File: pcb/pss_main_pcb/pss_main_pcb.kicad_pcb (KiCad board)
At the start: 2 copper layers, 177.8 x 55.9 mm, 96 parts, among them J1 24V DC Input, J2 220V AC Input, J3 Hot Air Gun, J4 Soldering Iron, J5 STM32_Prog, J6 UART_Prog, Q1 BC817, Q2 MMBT2222, Q3 MMBT2907, Q4 IRLML9301T, Q5 IRFZ44S, Q6 BT139B-800, SW1 Hot Air Gun Input, SW2 Soldering Iron Input, SW3 SW_Push, SW4 Main Encoder Input, SW5 EN, SW6 Boot, U1 LM2596S-5, U2 LM2596S-3.3, U3 MOC3023S, U4 LM358, U5 STM32F030K6Tx, U6 ESP32-WROOM-32U, U7 2.8inch_SPI_Module_ILI9341_SK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

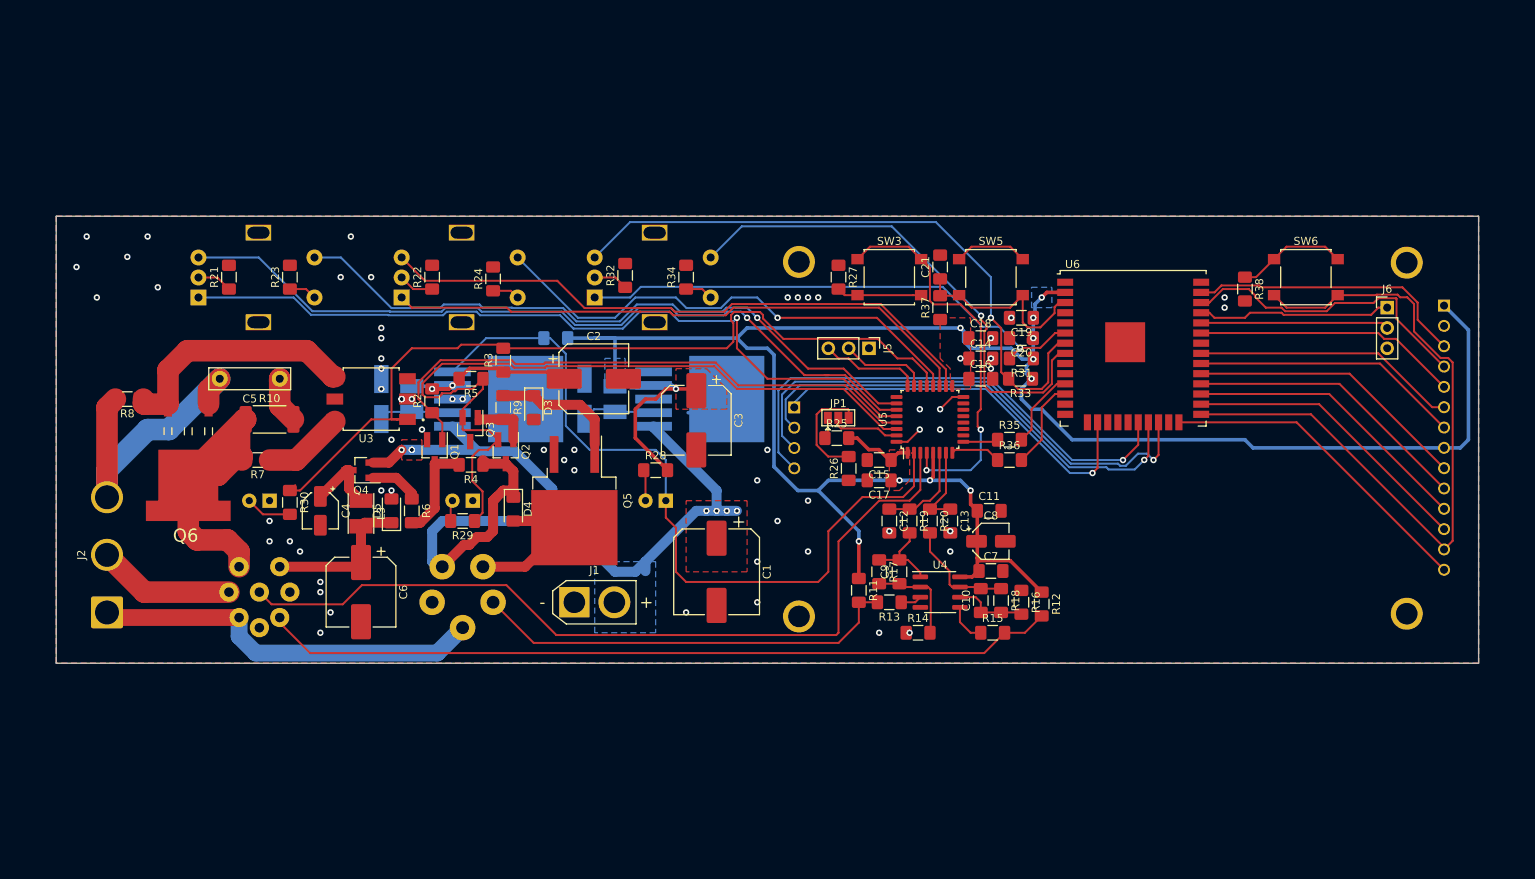
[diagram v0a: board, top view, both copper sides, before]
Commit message: Add 3D models and totaly redesign PCB
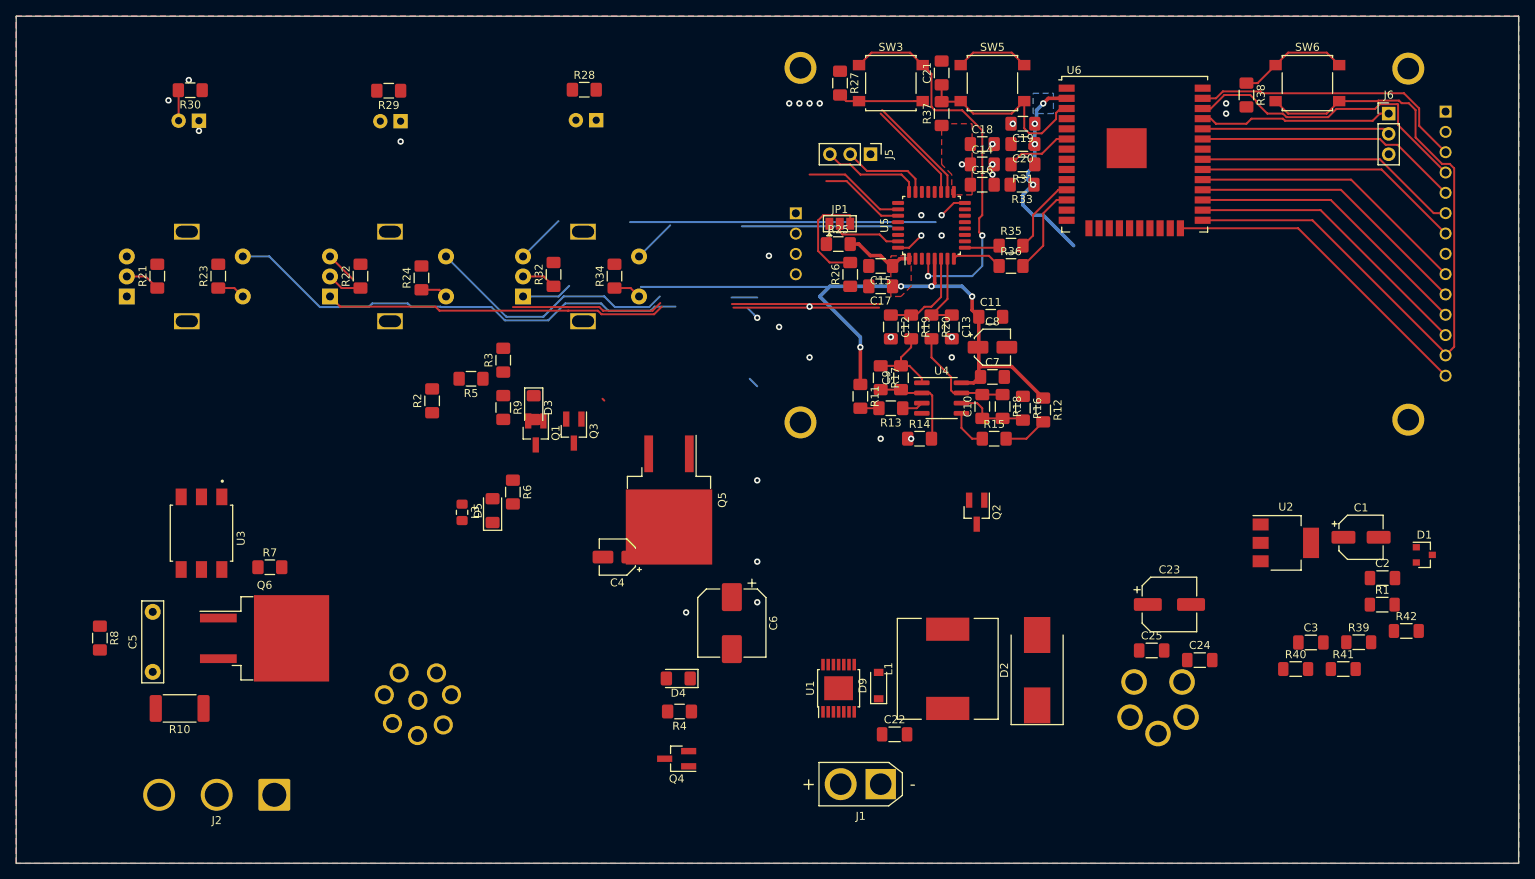
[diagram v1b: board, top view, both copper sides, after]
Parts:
- removed L2: 47u, Inductor_SMD:L_Taiyo-Yuden_NR-30xx_HandSoldering
- added C22: 0.68u, Capacitor_SMD:C_1206_3216Metric_Pad1.33x1.80mm_HandSolder, F.Cu at (164.5, 127.0)
- added C23: 100u 10v, Capacitor_SMD:CP_Elec_6.3x7.7, F.Cu at (198.8, 110.8)
- added C24: 0.47u, Capacitor_SMD:C_1206_3216Metric_Pad1.33x1.80mm_HandSolder, F.Cu at (202.6, 117.7)
- added C25: 33u, Capacitor_SMD:C_1206_3216Metric_Pad1.33x1.80mm_HandSolder, F.Cu at (196.6, 116.5)
- added D9: MMSD914T1, Diode_SMD:D_SOD-123, F.Cu at (162.5, 120.9)
- added R39: 10k, Resistor_SMD:R_1206_3216Metric_Pad1.30x1.75mm_HandSolder, F.Cu at (222.5, 115.5)
- added R40: 3.3k, Resistor_SMD:R_1206_3216Metric_Pad1.30x1.75mm_HandSolder, F.Cu at (214.6, 118.8)
- added R41: 15.4k, Resistor_SMD:R_1206_3216Metric_Pad1.30x1.75mm_HandSolder, F.Cu at (220.6, 118.8)
- added R42: 4.99k, Resistor_SMD:R_1206_3216Metric_Pad1.30x1.75mm_HandSolder, F.Cu at (228.5, 114.1)
- C1: value 470u 35V -> 4.7u 100v; footprint Capacitor_SMD:CP_Elec_10x10.5 -> Capacitor_SMD:CP_Elec_5x5.4
- C2: value 270u 10V -> 0.022u; footprint Capacitor_SMD:CP_Elec_8x10.5 -> Capacitor_SMD:C_1206_3216Metric_Pad1.33x1.80mm_HandSolder
- C3: value 330u 10V -> 220p; footprint Capacitor_SMD:CP_Elec_8x10.5 -> Capacitor_SMD:C_1206_3216Metric_Pad1.33x1.80mm_HandSolder
- C6: footprint Capacitor_SMD:CP_Elec_8x10.5 -> Capacitor_SMD:CP_Elec_8x10
- C8: footprint Capacitor_SMD:CP_Elec_4x5.4 -> Capacitor_SMD:CP_Elec_4x5.3
- D1: value SS34 -> MMBZ5233B-E3-08; footprint Diode_SMD:D_SMA_Handsoldering -> Package_TO_SOT_SMD:SOT-23; moved to F.Cu
- D2: value SS34 -> 30BQ060; footprint Diode_SMD:D_SMA_Handsoldering -> Diode_SMD:D_SMC_Handsoldering; moved to F.Cu
- L1: value 68u -> 22u; footprint Inductor_SMD:L_Taiyo-Yuden_NR-30xx_HandSoldering -> inductors:L_12x12mm_H8mm; moved to F.Cu
- L3: footprint Inductor_SMD:L_Taiyo-Yuden_NR-30xx_HandSoldering -> Inductor_SMD:L_0805_2012Metric_Pad1.15x1.40mm_HandSolder
- Q6: footprint bt139b:D2PAK-3 -> Package_TO_SOT_SMD:TO-263-2
- R1: value 1k -> 30k; footprint Resistor_SMD:R_1206_3216Metric_Pad1.42x1.75mm_HandSolder -> Resistor_SMD:R_1206_3216Metric_Pad1.30x1.75mm_HandSolder; moved to F.Cu
- SW1, SW2, SW4: footprint Rotary_Encoder:RotaryEncoder_Alps_EC11E-Switch_Vertical_H20mm -> encoders:RotaryEncoder_Alps_EC11E-Switch_Vertical_H20mm
- SW3, SW5, SW6: footprint Button_Switch_SMD:SW_SPST_B3S-1000 -> buttons:SW_SPST_B3S-1000
- U1: value LM2596S-5 -> LT3430; footprint Package_TO_SOT_SMD:TO-263-5_TabPin3 -> Package_SO:TSSOP-14-1EP_4.4x5mm_P0.65mm; moved to F.Cu
- U2: value LM2596S-3.3 -> LM3940IMP-3.3_NOPB; footprint Package_TO_SOT_SMD:TO-263-5_TabPin3 -> Package_TO_SOT_SMD:SOT-223; moved to F.Cu
- moved D1 131.8 mm to (230.7, 104.6), turned to 0 degrees
- moved R1 108.5 mm to (225.4, 110.8), turned to 0 degrees
- moved C2 101.7 mm to (225.5, 107.5)
- moved J4 88.1 mm to (197.4, 123.3)
- moved C3 81.7 mm to (216.5, 115.5), turned to 0 degrees
- moved C1 80.7 mm to (222.8, 102.4), turned to 0 degrees
- moved U2 75.4 mm to (213.4, 103.1)
- moved L1 75.0 mm to (171.1, 118.8), turned to 90 degrees
- moved D2 66.0 mm to (182.3, 119.0)
- moved Q2 59.3 mm to (174.8, 99.2)
- moved U1 55.8 mm to (157.5, 121.2), turned to 90 degrees
- moved R29 54.6 mm to (101.3, 46.5)
- moved Q4 53.5 mm to (137.2, 130.0)
- moved R30 53.0 mm to (76.4, 46.5), turned to 180 degrees
- moved R28 48.4 mm to (125.7, 46.4)
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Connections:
- C2 pad 1: +5V -> Net-(C2-Pad1)
- C3 pad 1: +3V3 -> Net-(C3-Pad1)
- D1 pad 1: Net-(D1-Pad1) -> GND
- D1 pad 2: GND -> (no net)
- D2 pad 1: Net-(D2-Pad1) -> SW
- L1 pad 1: +5V -> SW
- L1 pad 2: Net-(D1-Pad1) -> 5V
- R1 pad 1: +3V3 -> Iron_Heat_Pos
- R1 pad 2: Enable_5V -> SHDN
- R2 pad 2: +5V -> 5V
- R3 pad 1: +5V -> 5V
- R5 pad 2: +5V -> 5V
- U1 pad 1: Iron_Heat_Pos -> GND
- U1 pad 2: Net-(D1-Pad1) -> SW
- U1 pad 3: GND -> Iron_Heat_Pos
- U1 pad 4: +5V -> Iron_Heat_Pos
- U1 pad 5: Enable_5V -> SW
- U2 pad 1: Iron_Heat_Pos -> 5V
- U2 pad 2: Net-(D2-Pad1) -> GND
- U2 pad 3: GND -> +3V3
- U2 pad 4: +3V3 -> GND
- U3 pad 3: Net-(U3-Pad3) -> (no net)
- U3 pad 5: Net-(U3-Pad5) -> (no net)
- U5 pad 10: Net-(U5-Pad10) -> (no net)
- U5 pad 11: Net-(U5-Pad11) -> (no net)
- U5 pad 12: Net-(U5-Pad12) -> (no net)
- U5 pad 13: Net-(U5-Pad13) -> (no net)
- U5 pad 14: Net-(U5-Pad14) -> (no net)
- U5 pad 15: Net-(U5-Pad15) -> (no net)
- U5 pad 2: Enable_5V -> (no net)
- U5 pad 22: Net-(U5-Pad22) -> (no net)
- U5 pad 25: Net-(U5-Pad25) -> Enable_5V
- U6 pad 10: Net-(U6-Pad10) -> (no net)
- U6 pad 13: Net-(U6-Pad13) -> (no net)
- U6 pad 14: Net-(U6-Pad14) -> (no net)
- U6 pad 17: Net-(U6-Pad17) -> (no net)
- U6 pad 18: Net-(U6-Pad18) -> (no net)
- U6 pad 19: Net-(U6-Pad19) -> (no net)
- U6 pad 23: Net-(U6-Pad23) -> (no net)
- U6 pad 32: Net-(U6-Pad32) -> (no net)
- U6 pad 4: Net-(U6-Pad4) -> (no net)
- U6 pad 5: Net-(U6-Pad5) -> (no net)
- U6 pad 9: Net-(U6-Pad9) -> (no net)
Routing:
- net +3V3: track 288.5 -> 132.8 mm, vias 12 -> 9
- net Iron_Heat_Pos: track 120.9 -> 0.00 mm, vias 7 -> 0
- net Hot_Air_Reed: track 105.8 -> 0.10 mm
- net Heater_PWM: track 105.3 -> 0.00 mm
- net Sold_PWM: track 99.4 -> 0.00 mm
- net HotA_Enc_A: track 98.9 -> 0.75 mm, vias 1 -> 0
- net Enable_5V: track 97.8 -> 0.00 mm
- net Hot_Air_Therm_Pos: track 99.4 -> 5.52 mm
- net HotA_Enc_B: track 98.1 -> 10.8 mm, vias 1 -> 0
- net Fan_PWM: track 72.7 -> 0.00 mm
- net SD_SDO: track 64.7 -> 0.00 mm, vias 1 -> 0
- net SD_SCK: track 64.0 -> 0.00 mm, vias 1 -> 0
- net SD_SDI: track 59.3 -> 0.00 mm, vias 1 -> 0
- net Iron_Therm_Pos: track 53.7 -> 2.32 mm
- net Main_Enc_A: track 65.2 -> 14.6 mm, vias 1 -> 0
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- removed copper zone on B.Cu, net Iron_Heat_Pos
- removed copper zone on F.Cu, net Iron_Heat_Pos
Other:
- board size 177.8 x 55.9 mm -> 187.8 x 105.9 mm
